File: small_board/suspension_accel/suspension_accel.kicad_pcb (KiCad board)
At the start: 4 copper layers, 20 x 74 mm, 40 parts, among them IC1 TJA1050T_CM,118, IC2 AMS1117-3.3, IC3 SN74LVC1T45DCKR, IC4 ESP32-S3-MINI-1-N8, IC5 ADS1220IPWR, IC6 TLV75533PDBVR, IC7 SN74LVC1T45DCKR, J1 OSTTE040104, J2 BM04B-GVHS-TB_LF__SN_

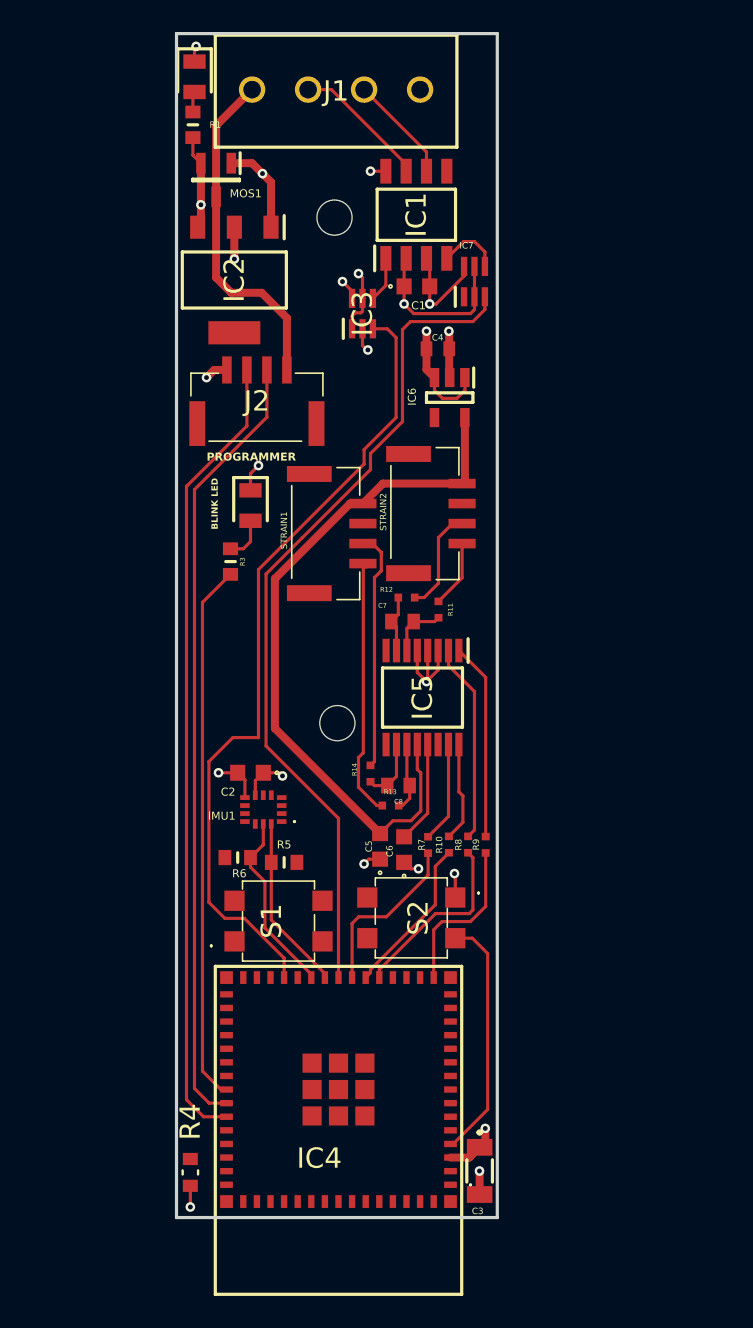
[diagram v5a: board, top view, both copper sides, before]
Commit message: added matched resistor network
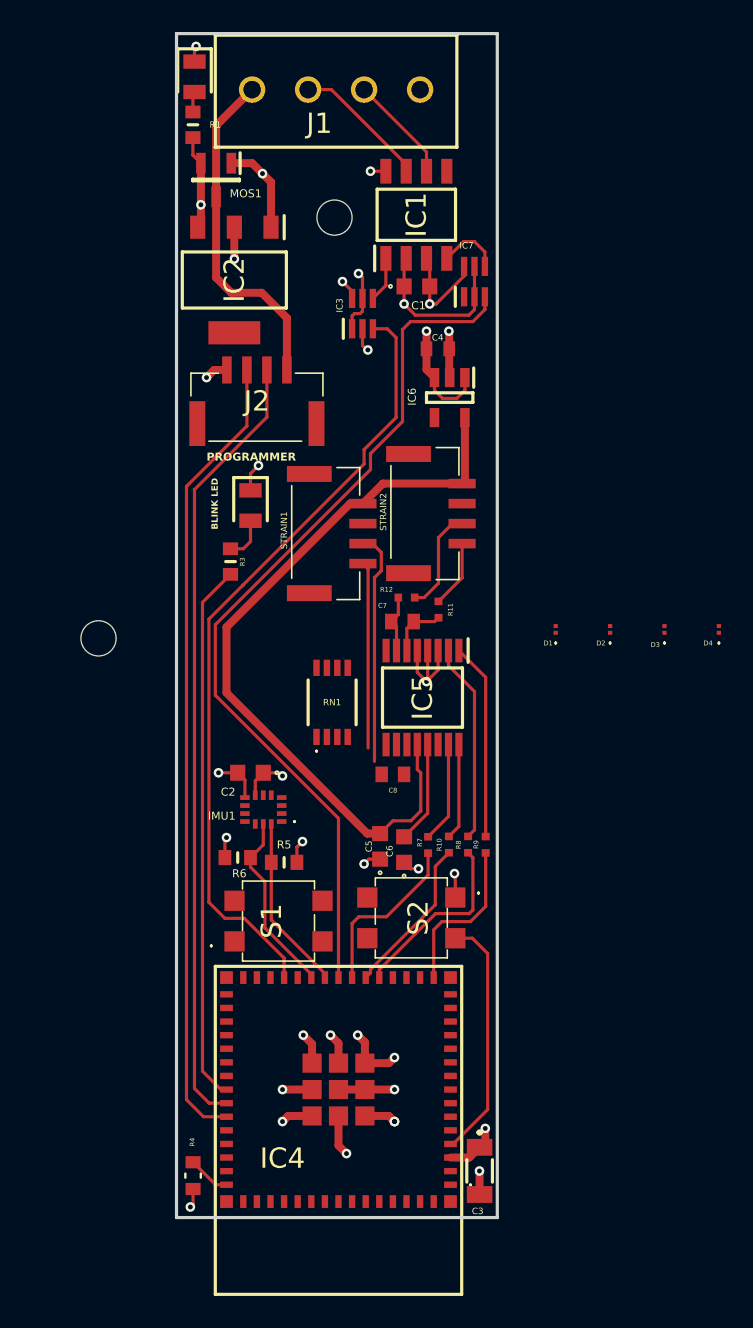
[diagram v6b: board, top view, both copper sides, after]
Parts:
- removed R13, R14: ERA-2AEB101X, Library:ERA2AED122X
- added D1: RCLAMP3521ZATFT, Library:RCLAMP3521ZATFT, F.Cu at (46.1, 61.2)
- added D2: RCLAMP3521ZATFT, Library:RCLAMP3521ZATFT, F.Cu at (49.5, 61.2)
- added D3: RCLAMP3521ZATFT, Library:RCLAMP3521ZATFT, F.Cu at (52.9, 61.2)
- added D4: RCLAMP3521ZATFT, Library:RCLAMP3521ZATFT, F.Cu at (56.3, 61.2)
- added RN1: MORNTA1001AT5, Library:MORNTA1001AT5, F.Cu at (32.1, 65.8)
- moved REF** 15.8 mm to (17.5, 61.8)
- moved C8 0.78 mm to (35.9, 70.3)
- moved R4 0.26 mm to (23.4, 95.4)
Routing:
- net GND: track 40.1 -> 60.0 mm, vias 14 -> 24
- net (no net): track 15.0 -> 0.00 mm
- net unconnected-(STRAIN1-Pad3): track 0.00 -> 14.6 mm
- net Net-(R13-Pad2): track 16.4 -> 11.7 mm
- net Net-(IC5-AIN0/REFP1): track 4.31 -> 0.00 mm
- net Net-(IC5-AIN1): track 3.97 -> 0.00 mm
- net /EXC+: track 55.1 -> 58.1 mm
- net Net-(IC4-IO19): track 52.4 -> 55.0 mm
- net +3.3V: track 20.1 -> 22.7 mm, vias 5 -> 7
- net Net-(IC4-EN): track 0.55 -> 2.67 mm
- net Net-(IC3-A): track 50.1 -> 49.2 mm

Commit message: started laying out final components
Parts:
- removed R11, R12: ERA-2AEB101X, Library:ERA2AED122X
- removed S1, S2: 7914G-1-032E, Library:7914G1032E
- moved D4 19.5 mm to (36.8, 60.9), turned to 180 degrees
- moved D3 16.5 mm to (36.5, 59.2), turned to -90 degrees
- moved REF** 12.0 mm to (29.2, 64.5)
- moved D2 8.85 mm to (41.0, 58.7), turned to -90 degrees
- moved C6 7.42 mm to (30.6, 70.7), turned to 180 degrees
- moved R10 7.15 mm to (34.4, 79.8)
- moved R8 7.08 mm to (35.7, 79.8)
- moved R7 6.93 mm to (33.4, 79.8)
- moved C7 6.30 mm to (36.8, 67.0)
- moved IC5 6.26 mm to (38.1, 71.8)
- moved D1 6.19 mm to (40.1, 59.5), turned to -90 degrees
- moved R9 6.12 mm to (38.5, 79.9)
- moved RN1 5.19 mm to (36.7, 63.4), turned to -90 degrees
- moved R6 5.05 mm to (27.2, 80.5)
- moved C8 4.62 mm to (32.4, 73.2)
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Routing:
- net /EXC+: track 58.1 -> 40.1 mm
- net Net-(IC4-IO0): track 15.6 -> 0.37 mm
- net Net-(R13-Pad2): track 11.7 -> 2.96 mm
- net Net-(IC4-IO16): track 11.6 -> 2.96 mm
- net GND: track 60.0 -> 51.9 mm, vias 24 -> 20
- net Net-(IC4-IO12): track 10.2 -> 2.60 mm
- net Net-(IC4-IO17): track 10.2 -> 2.77 mm
- net +3.3V: track 22.7 -> 15.3 mm, vias 7 -> 6
- net unconnected-(STRAIN1-Pad3): track 14.6 -> 8.55 mm
- net Net-(IC4-IO21): track 11.5 -> 7.37 mm
- net Net-(IC4-IO20): track 11.0 -> 7.43 mm
- net Net-(IC5-DIN): track 6.00 -> 9.00 mm
- net Net-(IC5-DOUT/~{DRDY}): track 6.29 -> 9.15 mm
- net Net-(D1-Pad1): track 6.55 -> 9.03 mm
- net Net-(IC5-~{CS}): track 12.5 -> 14.9 mm
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
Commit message: added ground pours and routed adc inputs
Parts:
- removed the REF** at (29.2, 64.5)
- removed the REF** at (32.2, 35.5)
- added REF**: TestPoint_Pad_1.0x1.0mm, TestPoint:TestPoint_Pad_1.0x1.0mm, F.Cu at (23.5, 92.8)
- moved C5 11.5 mm to (29.9, 65.6), turned to 0 degrees
- moved C7 9.58 mm to (36.0, 76.6)
- moved C8 7.70 mm to (37.0, 67.1), turned to 0 degrees
- moved D1 4.48 mm to (41.7, 55.3), turned to 180 degrees
- moved C6 3.25 mm to (32.5, 73.3)
- moved RN1 2.30 mm to (39.0, 62.9), turned to 180 degrees
- moved R9 1.80 mm to (40.1, 80.6), turned to 0 degrees
- moved D3 0.98 mm to (37.5, 59.1), turned to 0 degrees
- moved D4 0.97 mm to (36.0, 60.2)
- moved D2 0.81 mm to (40.2, 59.0)
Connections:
- net /EXC+ renamed Net-(IC4-IO18)
- C7 pad 1: Net-(IC5-AIN3/REFN1) -> Net-(IC5-AIN0/REFP1)
- C7 pad 2: Net-(IC5-AIN2) -> Net-(IC5-AIN1)
- C8 pad 1: Net-(IC5-AIN0/REFP1) -> Net-(IC5-AIN2)
- C8 pad 2: Net-(IC5-AIN1) -> Net-(IC5-AIN3/REFN1)
- D3 pad 1: unconnected-(D3-Pad1) -> Net-(D3-Pad1)
- D4 pad 1: unconnected-(D4-Pad1) -> Net-(D4-Pad1)
- RN1 pad 1: unconnected-(RN1-Pad1) -> Net-(D2-Pad1)
- RN1 pad 2: unconnected-(RN1-Pad2) -> Net-(D1-Pad1)
- RN1 pad 3: unconnected-(RN1-Pad3) -> Net-(D3-Pad1)
- RN1 pad 4: unconnected-(RN1-Pad4) -> Net-(D4-Pad1)
- RN1 pad 5: unconnected-(RN1-Pad5) -> Net-(IC5-AIN0/REFP1)
- RN1 pad 6: unconnected-(RN1-Pad6) -> Net-(IC5-AIN1)
- RN1 pad 7: unconnected-(RN1-Pad7) -> Net-(IC5-AIN2)
- RN1 pad 8: unconnected-(RN1-Pad8) -> Net-(IC5-AIN3/REFN1)
- STRAIN1 pad 3: unconnected-(STRAIN1-Pad3) -> Net-(D4-Pad1)
- STRAIN1 pad 4: Net-(R13-Pad2) -> Net-(D3-Pad1)
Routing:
- net GND: track 51.9 -> 34.6 mm, vias 20 -> 38
- net Net-(D4-Pad1): track 0.00 -> 9.53 mm
- net Net-(IC5-AIN1): track 0.00 -> 8.71 mm
- net unconnected-(STRAIN1-Pad3): track 8.55 -> 0.00 mm
- net Net-(IC5-AIN0/REFP1): track 0.00 -> 6.90 mm
- net Net-(D3-Pad1): track 0.00 -> 6.78 mm
- net Net-(IC5-AIN2): track 1.96 -> 6.12 mm
- net Net-(IC5-AIN3/REFN1): track 1.88 -> 5.43 mm
- net Net-(R13-Pad2): track 2.96 -> 0.00 mm
- net Net-(IC4-IO12): track 2.60 -> 0.00 mm
- net Net-(IC5-DOUT/~{DRDY}): track 9.15 -> 10.2 mm
- net Net-(IC5-DIN): track 9.00 -> 10.0 mm
- net Net-(IC5-~{CS}): track 14.9 -> 15.8 mm
- net Net-(D1-Pad1): track 9.03 -> 9.82 mm
- added copper zone on F.Cu, net GND
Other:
- board text added: "ENABLE TP"
